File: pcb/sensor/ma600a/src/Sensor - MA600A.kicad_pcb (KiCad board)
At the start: 2 copper layers, 22.3 x 20 mm, 6 parts, among them J1 781715006, U2 MA600A

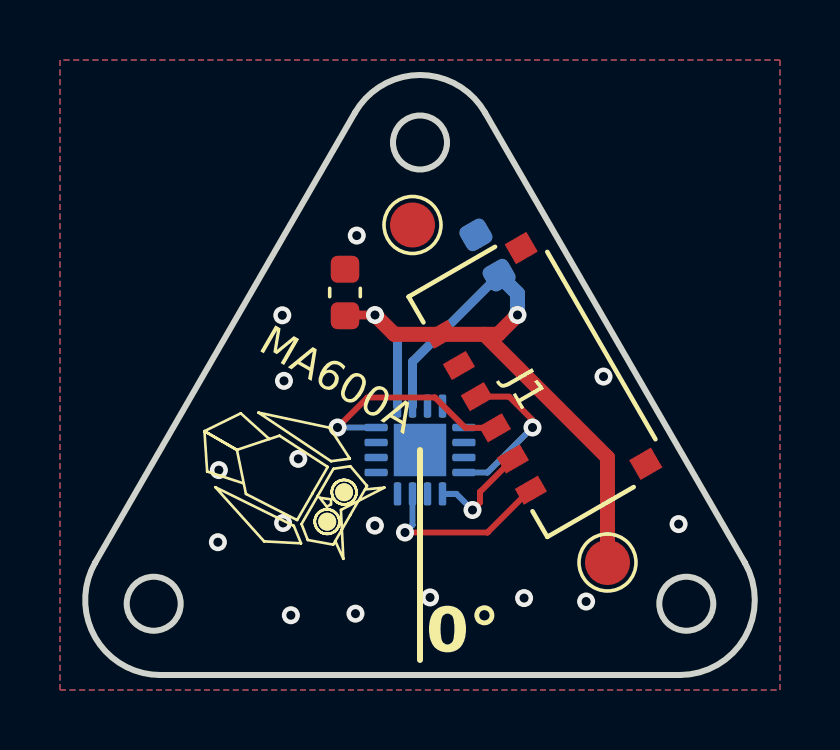
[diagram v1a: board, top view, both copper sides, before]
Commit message: Make the sensor mounting holes drilled NPTH holes
They were circles on Edge.Cuts, which got lost when the board was
panelized. Three board-only 1.8 mm NPTH footprints (H1-H3) now put them
in the drill file.

Co-Authored-By: Claude Opus 5 <noreply@anthropic.com>
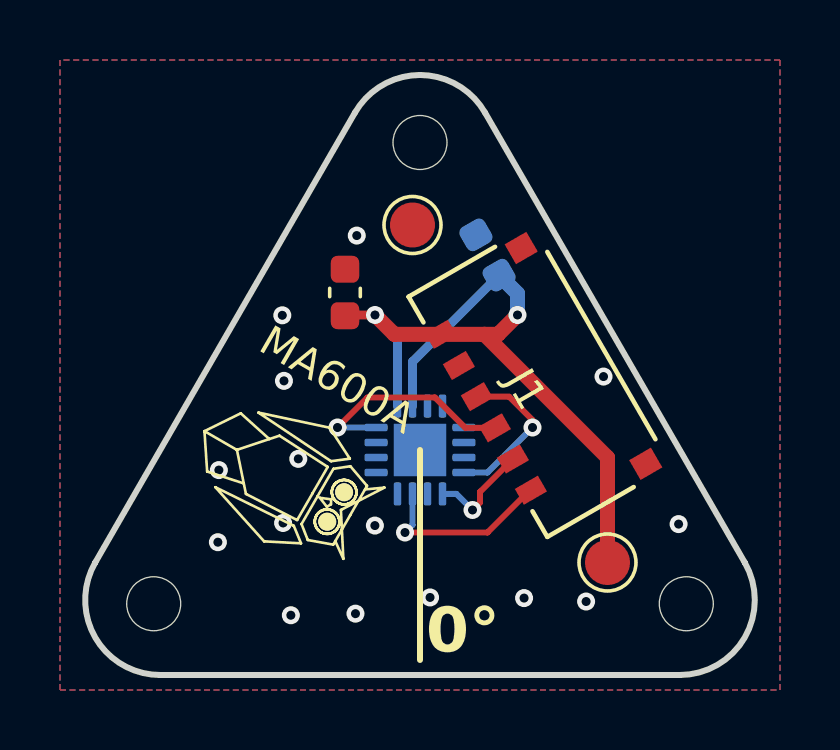
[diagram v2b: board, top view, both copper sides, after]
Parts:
- added H1: MountingHole_1.8mm_M1.6, MountingHole_1.8mm_M1.6, F.Cu at (150.0, 89.8)
- added H2: MountingHole_1.8mm_M1.6, MountingHole_1.8mm_M1.6, F.Cu at (141.1, 105.1)
- added H3: MountingHole_1.8mm_M1.6, MountingHole_1.8mm_M1.6, F.Cu at (158.9, 105.1)
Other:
- outline, holes or cut-outs redrawn
